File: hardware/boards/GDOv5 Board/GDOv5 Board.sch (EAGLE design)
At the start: 32 parts, among them IC1 DS1820, IC2 3.3V REG, J1 DCJ0202, Q1 BSS84, Q2 BSS138, Q3 BSS138, Q4 IRLML2502

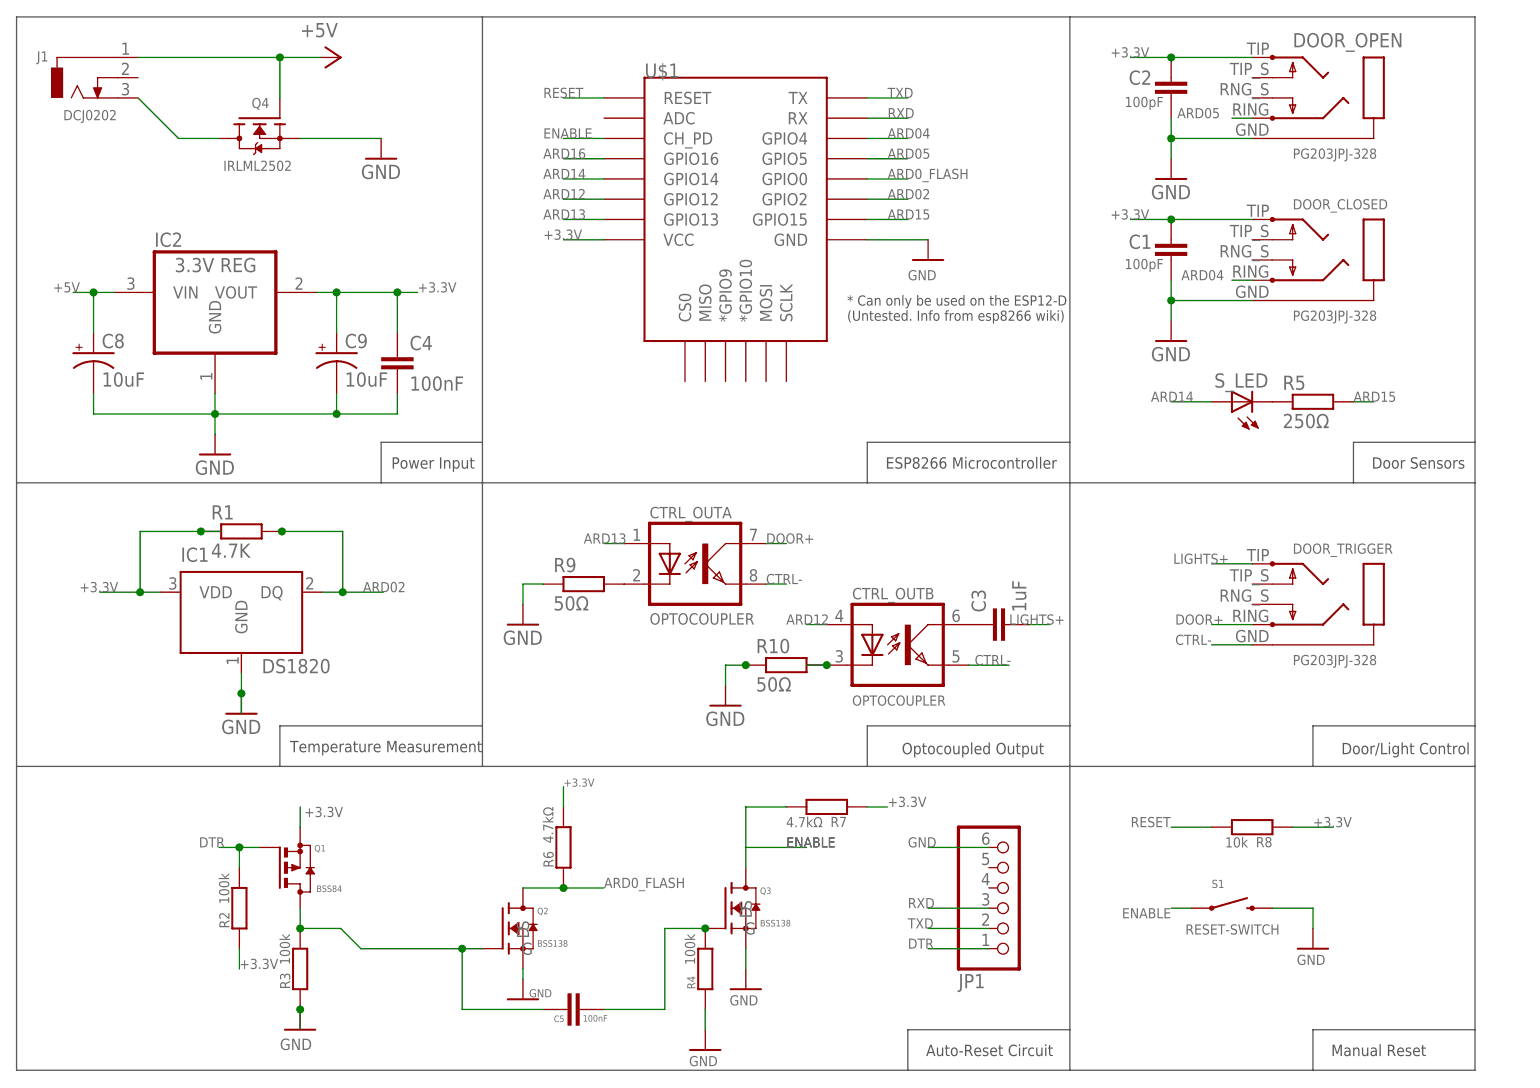
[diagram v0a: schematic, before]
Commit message: Board Design: Changed power supply buffer caps from 10µF to 22µF. Flipped Status LED connections for proper polarity. Added 10kΩ on GPIO15 to match with adapter board design on prototype.
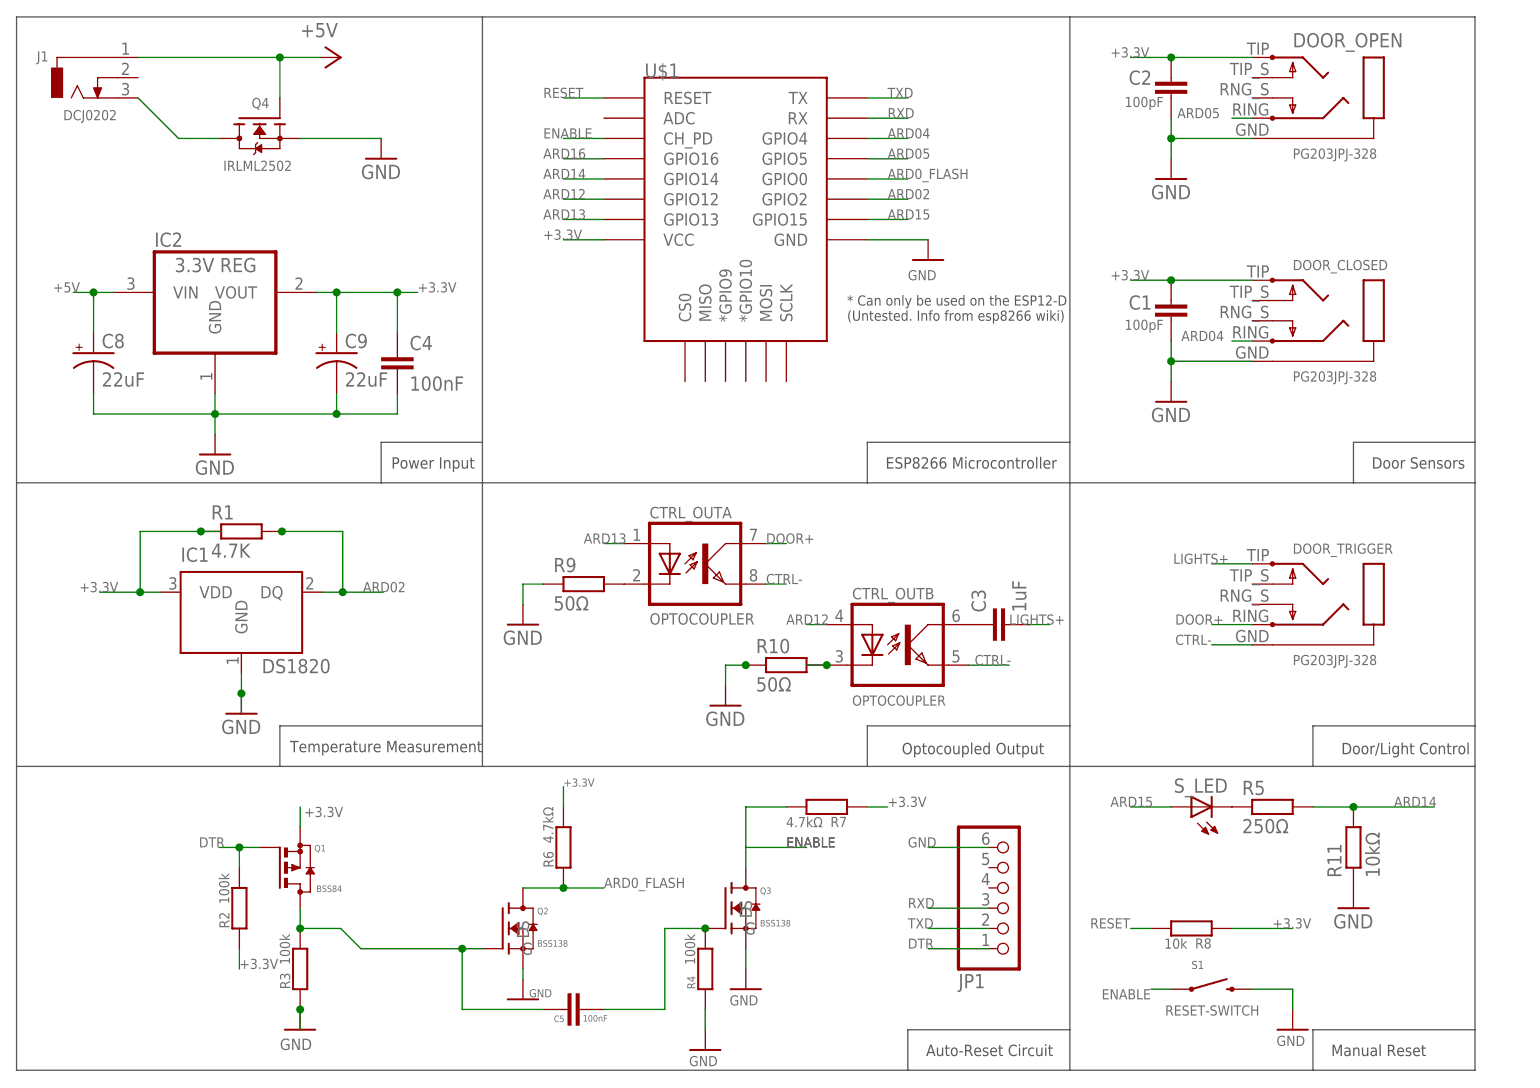
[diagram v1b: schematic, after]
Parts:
- added R11: 10kΩ, resistor:R-EU_M3216
- C8, C9: value 10uF -> 22uF
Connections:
- net ARD14: now also R11.2, R5.2; no longer S_LED.A
- net ARD15: now also S_LED.A; no longer R5.2
- net GND: now also R11.1
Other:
- moved on the sheet: C1, DOOR_CLOSED, R5, R8, S1, S_LED
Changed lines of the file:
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@@
 <part name="R10" library="resistor" deviceset="R-EU_" device="M3216" value="50Ω"/>
 <part name="GND13" library="supply1" deviceset="GND" device=""/>
-<part name="C8" library="SparkFun-Capacitors" deviceset="10UF-TANT" device="" value="10uF"/>
-<part name="C9" library="SparkFun-Capacitors" deviceset="10UF-TANT" device="" value="10uF"/>
+<part name="C8" library="SparkFun-Capacitors" deviceset="10UF-TANT" device="" value="22uF"/>
+<part name="C9" library="SparkFun-Capacitors" deviceset="10UF-TANT" device="" value="22uF"/>
 <part name="C4" library="resistor" deviceset="C-EU" device="C1206" value="100nF"/>
 <part name="C3" library="SparkFun-Capacitors" deviceset="CAP" device="1206" value="1uF"/>
@@
 <part name="R8" library="resistor" deviceset="R-EU_" device="M3216" value="10k"/>
 <part name="GND6" library="supply1" deviceset="GND" device=""/>
+<part name="R11" library="resistor" deviceset="R-EU_" device="M3216" value="10kΩ"/>
+<part name="GND14" library="supply1" deviceset="GND" device=""/>
 </parts>
 <sheets>
@@
 <attribute name="VALUE" x="129.54" y="96.52" size="1.27" layer="96"/>
 </instance>
-<instance part="DOOR_CLOSED" gate="1" x="137.16" y="86.36" smashed="yes">
-<attribute name="NAME" x="129.54" y="90.17" size="1.27" layer="95"/>
-<attribute name="VALUE" x="129.54" y="76.2" size="1.27" layer="96"/>
+<instance part="DOOR_CLOSED" gate="1" x="137.16" y="78.74" smashed="yes">
+<attribute name="NAME" x="129.54" y="82.55" size="1.27" layer="95"/>
+<attribute name="VALUE" x="129.54" y="68.58" size="1.27" layer="96"/>
 </instance>
 <instance part="DOOR_TRIGGER" gate="1" x="137.16" y="43.18" smashed="yes">
@@
 <instance part="IC2" gate="G$1" x="-5.588" y="79.756"/>
 <instance part="GND2" gate="1" x="-5.588" y="59.436"/>
-<instance part="GND3" gate="1" x="114.3" y="73.66"/>
+<instance part="GND3" gate="1" x="114.3" y="66.04"/>
 <instance part="GND4" gate="1" x="114.3" y="93.98"/>
-<instance part="C1" gate="G$1" x="114.3" y="86.36" smashed="yes">
-<attribute name="NAME" x="108.966" y="85.217" size="1.778" layer="95"/>
-<attribute name="VALUE" x="108.458" y="82.677" size="1.27" layer="96"/>
+<instance part="C1" gate="G$1" x="114.3" y="78.74" smashed="yes">
+<attribute name="NAME" x="108.966" y="77.597" size="1.778" layer="95"/>
+<attribute name="VALUE" x="108.458" y="75.057" size="1.27" layer="96"/>
 </instance>
 <instance part="C2" gate="G$1" x="114.3" y="106.68" smashed="yes">
@@
 <instance part="R1" gate="G$1" x="-2.286" y="49.784"/>
 <instance part="JP1" gate="A" x="93.98" y="5.08" rot="MR180"/>
-<instance part="S_LED" gate="G$1" x="121.92" y="66.04" rot="R90"/>
-<instance part="R5" gate="G$1" x="132.08" y="66.04"/>
+<instance part="S_LED" gate="G$1" x="116.84" y="15.24" rot="R90"/>
+<instance part="R5" gate="G$1" x="127" y="15.24"/>
 <instance part="GND12" gate="1" x="-2.286" y="26.924"/>
 <instance part="R9" gate="G$1" x="40.64" y="43.18"/>
@@
 <attribute name="VALUE" x="36.83" y="10.668" size="1.27" layer="96" rot="R90"/>
 </instance>
-<instance part="S1" gate="G$1" x="121.92" y="2.54" smashed="yes">
-<attribute name="NAME" x="119.38" y="5.08" size="1.016" layer="95"/>
-<attribute name="VALUE" x="116.078" y="-0.762" size="1.27" layer="96"/>
-</instance>
-<instance part="GND11" gate="1" x="132.08" y="-2.54" smashed="yes">
-<attribute name="VALUE" x="130.048" y="-4.572" size="1.27" layer="96"/>
+<instance part="S1" gate="G$1" x="119.38" y="-7.62" smashed="yes">
+<attribute name="NAME" x="116.84" y="-5.08" size="1.016" layer="95"/>
+<attribute name="VALUE" x="113.538" y="-10.922" size="1.27" layer="96"/>
+</instance>
+<instance part="GND11" gate="1" x="129.54" y="-12.7" smashed="yes">
+<attribute name="VALUE" x="127.508" y="-14.732" size="1.27" layer="96"/>
 </instance>
 <instance part="P+1" gate="1" x="10.16" y="109.22" rot="R270"/>
@@
 <attribute name="VALUE" x="70.612" y="13.97" size="1.27" layer="96" rot="R180"/>
 </instance>
-<instance part="R8" gate="G$1" x="124.46" y="12.7" smashed="yes" rot="R180">
-<attribute name="NAME" x="127" y="11.4554" size="1.27" layer="95" rot="R180"/>
-<attribute name="VALUE" x="123.952" y="11.43" size="1.27" layer="96" rot="R180"/>
+<instance part="R8" gate="G$1" x="116.84" y="0" smashed="yes" rot="R180">
+<attribute name="NAME" x="119.38" y="-1.2446" size="1.27" layer="95" rot="R180"/>
+<attribute name="VALUE" x="116.332" y="-1.27" size="1.27" layer="96" rot="R180"/>
 </instance>
 <instance part="GND6" gate="1" x="55.88" y="-15.24" smashed="yes">
 <attribute name="VALUE" x="53.848" y="-17.272" size="1.27" layer="96"/>
+</instance>
+<instance part="R11" gate="G$1" x="137.16" y="10.16" rot="R90"/>
+<instance part="GND14" gate="1" x="137.16" y="2.54" smashed="yes">
+<attribute name="VALUE" x="134.62" y="0" size="1.778" layer="96"/>
 </instance>
 </instances>
@@
 <segment>
 <pinref part="DOOR_CLOSED" gate="1" pin="1"/>
-<wire x1="124.46" y1="78.74" x2="114.3" y2="78.74" width="0.1524" layer="91"/>
-<wire x1="114.3" y1="78.74" x2="114.3" y2="76.2" width="0.1524" layer="91"/>
+<wire x1="124.46" y1="71.12" x2="114.3" y2="71.12" width="0.1524" layer="91"/>
+<wire x1="114.3" y1="71.12" x2="114.3" y2="68.58" width="0.1524" layer="91"/>
 <pinref part="GND3" gate="1" pin="GND"/>
 <pinref part="C1" gate="G$1" pin="2"/>
-<wire x1="114.3" y1="81.28" x2="114.3" y2="78.74" width="0.1524" layer="91"/>
-<junction x="114.3" y="78.74"/>
+<wire x1="114.3" y1="73.66" x2="114.3" y2="71.12" width="0.1524" layer="91"/>
+<junction x="114.3" y="71.12"/>
 </segment>
 <segment>
@@
 <segment>
 <pinref part="S1" gate="G$1" pin="2"/>
-<wire x1="127" y1="2.54" x2="132.08" y2="2.54" width="0.1524" layer="91"/>
-<wire x1="132.08" y1="2.54" x2="132.08" y2="0" width="0.1524" layer="91"/>
+<wire x1="124.46" y1="-7.62" x2="129.54" y2="-7.62" width="0.1524" layer="91"/>
+<wire x1="129.54" y1="-7.62" x2="129.54" y2="-10.16" width="0.1524" layer="91"/>
 <pinref part="GND11" gate="1" pin="GND"/>
 </segment>
@@
 <wire x1="55.88" y1="-10.16" x2="55.88" y2="-12.7" width="0.1524" layer="91"/>
 <pinref part="GND6" gate="1" pin="GND"/>
+</segment>
+<segment>
+<pinref part="R11" gate="G$1" pin="1"/>
+<pinref part="GND14" gate="1" pin="GND"/>
 </segment>
 </net>
@@
 <segment>
 <pinref part="DOOR_CLOSED" gate="1" pin="5"/>
-<wire x1="124.46" y1="88.9" x2="114.3" y2="88.9" width="0.1524" layer="91"/>
+<wire x1="124.46" y1="81.28" x2="114.3" y2="81.28" width="0.1524" layer="91"/>
 <pinref part="C1" gate="G$1" pin="1"/>
-<wire x1="114.3" y1="88.9" x2="109.22" y2="88.9" width="0.1524" layer="91"/>
-<junction x="114.3" y="88.9"/>
-<label x="106.68" y="88.9" size="1.27" layer="95"/>
+<wire x1="114.3" y1="81.28" x2="109.22" y2="81.28" width="0.1524" layer="91"/>
+<junction x="114.3" y="81.28"/>
+<label x="106.68" y="81.28" size="1.27" layer="95"/>
 </segment>
 <segment>
@@
 <segment>
 <pinref part="R8" gate="G$1" pin="1"/>
-<wire x1="129.54" y1="12.7" x2="134.62" y2="12.7" width="0.1524" layer="91"/>
-<label x="132.08" y="12.7" size="1.27" layer="95"/>
+<wire x1="121.92" y1="0" x2="129.54" y2="0" width="0.1524" layer="91"/>
+<label x="127" y="0" size="1.27" layer="95"/>
 </segment>
 </net>
@@
 <segment>
 <pinref part="DOOR_CLOSED" gate="1" pin="2"/>
-<wire x1="124.46" y1="81.28" x2="121.92" y2="81.28" width="0.1524" layer="91"/>
-<label x="115.57" y="81.28" size="1.27" layer="95"/>
+<wire x1="124.46" y1="73.66" x2="121.92" y2="73.66" width="0.1524" layer="91"/>
+<label x="115.57" y="73.66" size="1.27" layer="95"/>
 </segment>
 <segment>
@@
 </segment>
 <segment>
-<pinref part="S_LED" gate="G$1" pin="A"/>
-<wire x1="119.38" y1="66.04" x2="114.3" y2="66.04" width="0.1524" layer="91"/>
-<label x="111.76" y="66.04" size="1.27" layer="95"/>
+<pinref part="R5" gate="G$1" pin="2"/>
+<wire x1="132.08" y1="15.24" x2="137.16" y2="15.24" width="0.1524" layer="91"/>
+<label x="142.24" y="15.24" size="1.27" layer="95"/>
+<pinref part="R11" gate="G$1" pin="2"/>
+<wire x1="137.16" y1="15.24" x2="147.32" y2="15.24" width="0.1524" layer="91"/>
+<junction x="137.16" y="15.24"/>
 </segment>
 </net>
@@
 <segment>
 <pinref part="S1" gate="G$1" pin="1"/>
-<wire x1="116.84" y1="2.54" x2="114.3" y2="2.54" width="0.1524" layer="91"/>
-<label x="114.3" y="2.54" size="1.27" layer="95" rot="R180"/>
+<wire x1="114.3" y1="-7.62" x2="111.76" y2="-7.62" width="0.1524" layer="91"/>
+<label x="111.76" y="-7.62" size="1.27" layer="95" rot="R180"/>
 </segment>
 </net>
@@
 </segment>
 <segment>
-<wire x1="114.3" y1="12.7" x2="119.38" y2="12.7" width="0.1524" layer="91"/>
+<wire x1="109.22" y1="0" x2="111.76" y2="0" width="0.1524" layer="91"/>
 <pinref part="R8" gate="G$1" pin="2"/>
-<label x="109.22" y="12.7" size="1.27" layer="95"/>
+<label x="104.14" y="0" size="1.27" layer="95"/>
 </segment>
 </net>
@@
 </segment>
 <segment>
-<pinref part="R5" gate="G$1" pin="2"/>
-<wire x1="137.16" y1="66.04" x2="139.7" y2="66.04" width="0.1524" layer="91"/>
-<label x="137.16" y="66.04" size="1.27" layer="95"/>
-</segment>
-</net>
+<pinref part="S_LED" gate="G$1" pin="A"/>
+<wire x1="114.3" y1="15.24" x2="109.22" y2="15.24" width="0.1524" layer="91"/>
+<label x="106.68" y="15.24" size="1.27" layer="95"/>
+</segment>
+</net>
